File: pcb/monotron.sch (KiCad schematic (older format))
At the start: 44 parts, among them J1 Mono / Stereo, J10 DIN-5_180degree, J11 DIN-5_180degree, J12 DB9_Male, J2 Jack-DC, J3 01x07 SD Interface, J4 AudioJack3, J5 DB9_Male, J6 1x4 I2C Expansion Connector, J7 DB15_Female_HighDensity_Mount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, J8 2x6 UART Bridge, J9 DIN-5_180degree, U1 TM4C123G_Launchpad, U2 MAX3232, U3 74LS14, U4 6N138

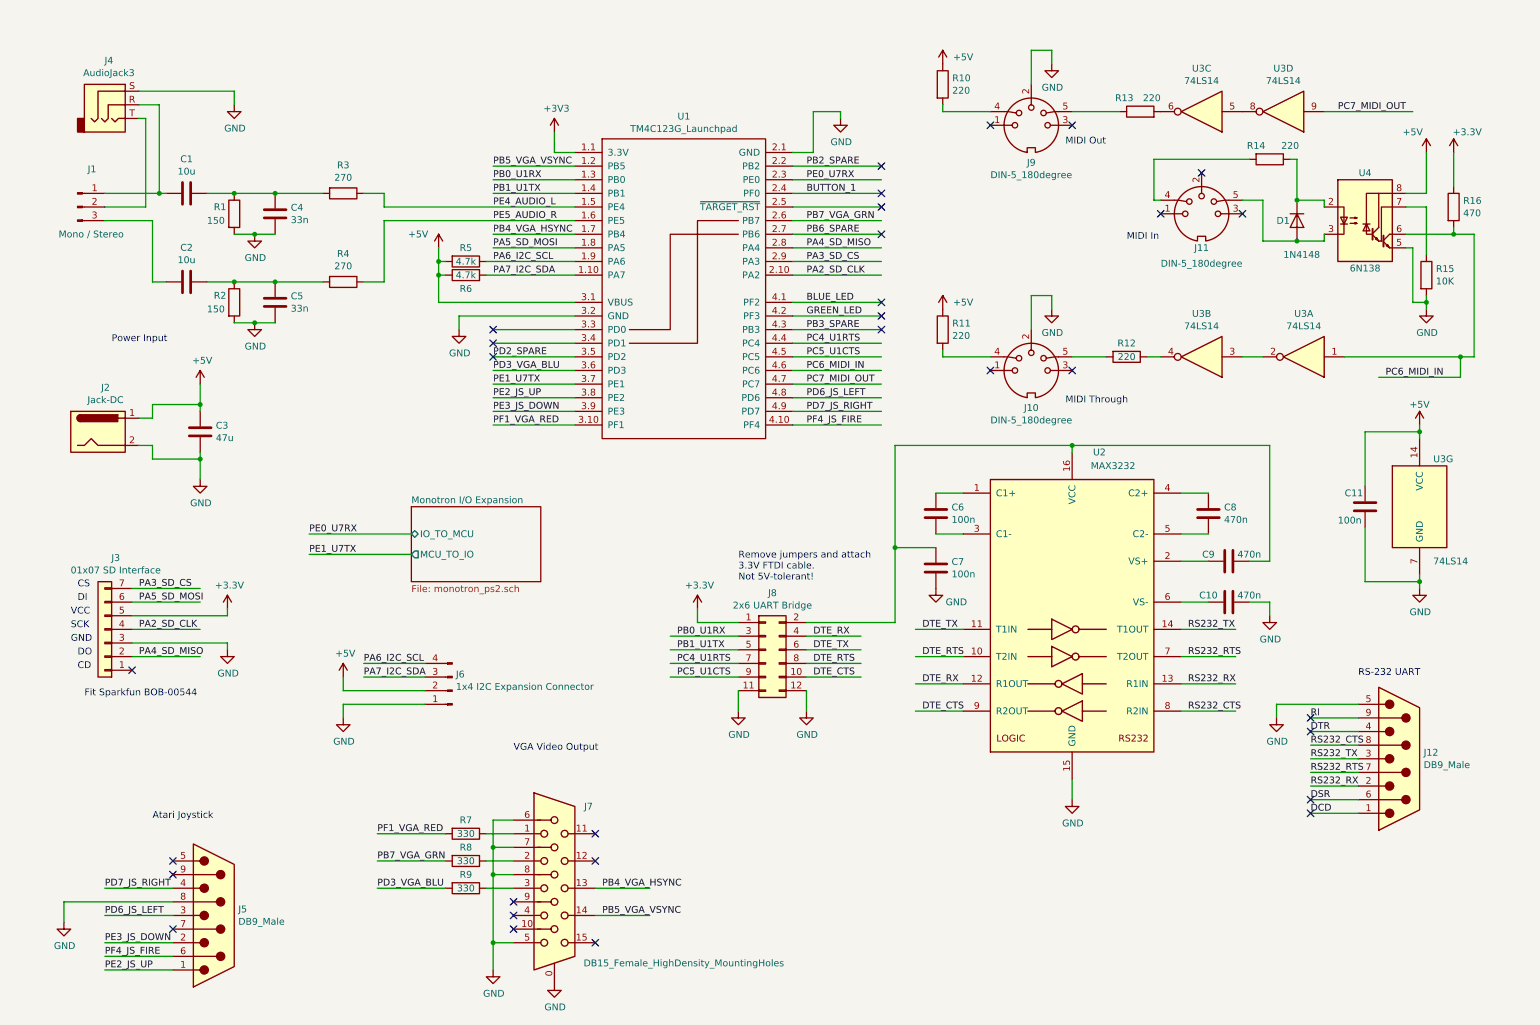
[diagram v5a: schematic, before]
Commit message: Updated footprints.
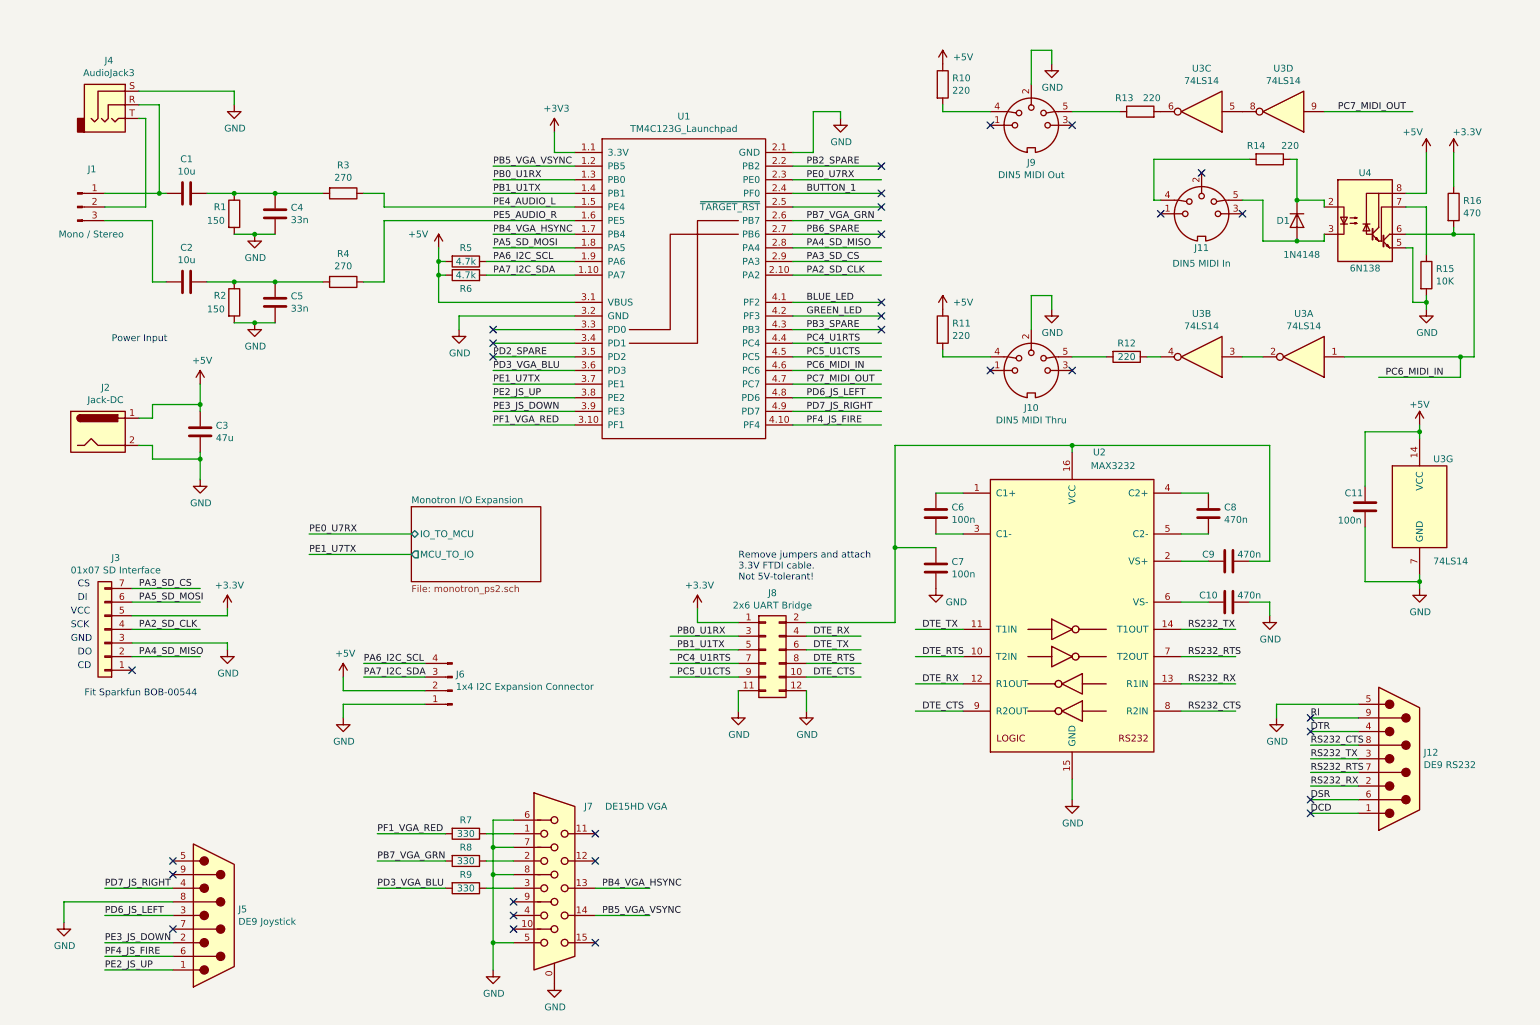
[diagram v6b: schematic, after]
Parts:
- D1: footprint (none) -> Diode_THT:D_A-405_P12.70mm_Horizontal
- J10: value DIN-5_180degree -> DIN5 MIDI Thru; footprint (none) -> Launchpad:5P180 DIN Socket
- J11: value DIN-5_180degree -> DIN5 MIDI In; footprint (none) -> Launchpad:5P180 DIN Socket
- J12: value DB9_Male -> DE9 RS232
- J4: Digikey (none) -> CP1-3533NG-ND‎
- J5: value DB9_Male -> DE9 Joystick
- J7: value DB15_Female_HighDensity_MountingHoles -> DE15HD VGA
- J9: value DIN-5_180degree -> DIN5 MIDI Out; footprint (none) -> Launchpad:5P180 DIN Socket
- R10, R11, R12, R13, R14, R15, R16: footprint (none) -> Resistor_THT:R_Axial_DIN0411_L9.9mm_D3.6mm_P12.70mm_Horizontal
- U3: footprint (none) -> Package_DIP:DIP-14_W7.62mm; Digikey (none) -> 296-1643-5-ND
- U3: footprint (none) -> Package_DIP:DIP-14_W7.62mm
- U4: footprint (none) -> Package_DIP:DIP-8_W7.62mm
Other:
- note removed: "Atari Joystick"
- note removed: "MIDI In"
- note removed: "MIDI Out"
- note removed: "MIDI Through"
- note removed: "RS-232 UART"
- note removed: "VGA Video Output"
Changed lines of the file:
@@
 P 1850 6900
 F 0 "J5" H 2030 6946 50  0000 L CNN
-F 1 "DB9_Male" H 2030 6855 50  0000 L CNN
+F 1 "DE9 Joystick" H 2030 6855 50  0000 L CNN
 F 2 "Connector_Dsub:DSUB-9_Male_Horizontal_P2.77x2.84mm_EdgePinOffset7.70mm_Housed_MountingHolesOffset9.12mm" H 1850 6900 50  0001 C CNN
 F 3 " http://portal.fciconnect.com/Comergent//fci/drawing/c-dd-0024.pdf" H 1850 6900 50  0001 C CNN
@@
 	1    0    0    -1
 $EndComp
-Text Notes 1400 6200 0    50   ~ 0
-Atari Joystick
 Text Label 1050 7300 0    50   ~ 0
 PE2_JS_UP
@@
 P 4350 6700
 F 0 "J7" H 4600 7300 50  0000 C CNN
-F 1 "DB15_Female_HighDensity_MountingHoles" H 5300 6150 50  0000 C CNN
+F 1 "DE15HD VGA" H 4950 7300 50  0000 C CNN
 F 2 "Connector_Dsub:DSUB-15-HD_Female_Horizontal_P2.29x1.98mm_EdgePinOffset8.35mm_Housed_MountingHolesOffset10.89mm" H 3400 7100 50  0001 C CNN
 F 3 "https://www.amphenol-icc.com/media/wysiwyg/files/drawing/c-cd-0012.pdf" H 3400 7100 50  0001 C CNN
@@
 F 2 "Connector_Audio:Jack_3.5mm_CUI_SJ1-3533NG_Horizontal" H 1100 950 50  0001 C CNN
 F 3 "~" H 1100 950 50  0001 C CNN
+F 4 "CP1-3533NG-ND‎" H 1100 950 50  0001 C CNN "Digikey"
 	1    1100 950
 	1    0    0    -1
@@
 AR Path="/5C4BB195" Ref="J12"  Part="1"
 F 0 "J12" H 10730 5796 50  0000 L CNN
-F 1 "DB9_Male" H 10730 5705 50  0000 L CNN
+F 1 "DE9 RS232" H 10730 5705 50  0000 L CNN
 F 2 "Connector_Dsub:DSUB-9_Male_Horizontal_P2.77x2.84mm_EdgePinOffset7.70mm_Housed_MountingHolesOffset9.12mm" H 10550 5750 50  0001 C CNN
 F 3 "http://portal.fciconnect.com/Comergent//fci/drawing/c-dd-0024.pdf" H 10550 5750 50  0001 C CNN
@@
 Text Notes 5700 4450 0    50   ~ 0
 Remove jumpers and attach\n3.3V FTDI cable.\nNot 5V-tolerant!
-Text Notes 4050 5700 0    50   ~ 0
-VGA Video Output
-Text Notes 10250 5150 0    50   ~ 0
-RS-232 UART
 Text Label 3900 2800 0    50   ~ 0
 PD2_SPARE
@@
 P 7850 1100
 F 0 "J9" H 7850 826 50  0000 C CNN
-F 1 "DIN-5_180degree" H 7850 735 50  0000 C CNN
-F 2 "" H 7850 1100 50  0001 C CNN
-F 3 "http://www.mouser.com/ds/2/18/40_c091_abd_e-75918.pdf" H 7850 1100 50  0001 C CNN
+F 1 "DIN5 MIDI Out" H 7850 735 50  0000 C CNN
+F 2 "Launchpad:5P180 DIN Socket" H 7850 1100 50  0001 C CNN
+F 3 "https://uk.rs-online.com/web/p/din-connectors/0491087/" H 7850 1100 50  0001 C CNN
 	1    7850 1100
 	1    0    0    -1
@@
 P 9100 1750
 F 0 "J11" H 9100 1500 50  0000 C CNN
-F 1 "DIN-5_180degree" H 9100 1385 50  0000 C CNN
-F 2 "" H 9100 1750 50  0001 C CNN
-F 3 "http://www.mouser.com/ds/2/18/40_c091_abd_e-75918.pdf" H 9100 1750 50  0001 C CNN
+F 1 "DIN5 MIDI In" H 9100 1385 50  0000 C CNN
+F 2 "Launchpad:5P180 DIN Socket" H 9100 1750 50  0001 C CNN
+F 3 "https://uk.rs-online.com/web/p/din-connectors/0491087/" H 9100 1750 50  0001 C CNN
 	1    9100 1750
 	1    0    0    -1
 $EndComp
-Text Notes 8100 1250 0    50   ~ 0
-MIDI Out
-Text Notes 8550 1950 0    50   ~ 0
-MIDI In
 $Comp
 L Connector:DIN-5_180degree J10
@@
 P 7850 2900
 F 0 "J10" H 7850 2626 50  0000 C CNN
-F 1 "DIN-5_180degree" H 7850 2535 50  0000 C CNN
-F 2 "" H 7850 2900 50  0001 C CNN
-F 3 "http://www.mouser.com/ds/2/18/40_c091_abd_e-75918.pdf" H 7850 2900 50  0001 C CNN
+F 1 "DIN5 MIDI Thru" H 7850 2535 50  0000 C CNN
+F 2 "Launchpad:5P180 DIN Socket" H 7850 2900 50  0001 C CNN
+F 3 "https://uk.rs-online.com/web/p/din-connectors/0491087/" H 7850 2900 50  0001 C CNN
 	1    7850 2900
 	1    0    0    -1
 $EndComp
-Text Notes 8100 3150 0    50   ~ 0
-MIDI Through
 NoConn ~ 7550 2900
 NoConn ~ 8150 2900
@@
 F 0 "R11" H 7270 2646 50  0000 L CNN
 F 1 "220" H 7270 2555 50  0000 L CNN
-F 2 "" V 7130 2600 50  0001 C CNN
+F 2 "Resistor_THT:R_Axial_DIN0411_L9.9mm_D3.6mm_P12.70mm_Horizontal" V 7130 2600 50  0001 C CNN
 F 3 "~" H 7200 2600 50  0001 C CNN
 	1    7200 2600
@@
 F 0 "R10" H 7270 846 50  0000 L CNN
 F 1 "220" H 7270 755 50  0000 L CNN
-F 2 "" V 7130 800 50  0001 C CNN
+F 2 "Resistor_THT:R_Axial_DIN0411_L9.9mm_D3.6mm_P12.70mm_Horizontal" V 7130 800 50  0001 C CNN
 F 3 "~" H 7200 800 50  0001 C CNN
 	1    7200 800
@@
 F 0 "U4" H 10300 2150 50  0000 C CNN
 F 1 "6N138" H 10300 1450 50  0000 C CNN
-F 2 "" H 10590 1500 50  0001 C CNN
+F 2 "Package_DIP:DIP-8_W7.62mm" H 10590 1500 50  0001 C CNN
 F 3 "http://www.onsemi.com/pub/Collateral/HCPL2731-D.pdf" H 10590 1500 50  0001 C CNN
 	1    10300 1800
@@
 F 0 "R14" V 9500 1250 50  0000 C CNN
 F 1 "220" V 9500 1500 50  0000 C CNN
-F 2 "" V 9530 1350 50  0001 C CNN
+F 2 "Resistor_THT:R_Axial_DIN0411_L9.9mm_D3.6mm_P12.70mm_Horizontal" V 9530 1350 50  0001 C CNN
 F 3 "~" H 9600 1350 50  0001 C CNN
 	1    9600 1350
@@
 F 0 "D1" V 9800 1650 50  0000 L CNN
 F 1 "1N4148" V 10050 1700 50  0000 L CNN
-F 2 "" H 9800 1800 50  0001 C CNN
+F 2 "Diode_THT:D_A-405_P12.70mm_Horizontal" H 9800 1800 50  0001 C CNN
 F 3 "~" H 9800 1800 50  0001 C CNN
 	1    9800 1800
@@
 F 0 "R15" H 10820 2246 50  0000 L CNN
 F 1 "10K" H 10820 2155 50  0000 L CNN
-F 2 "" V 10680 2200 50  0001 C CNN
+F 2 "Resistor_THT:R_Axial_DIN0411_L9.9mm_D3.6mm_P12.70mm_Horizontal" V 10680 2200 50  0001 C CNN
 F 3 "~" H 10750 2200 50  0001 C CNN
 	1    10750 2200
@@
 F 0 "R16" H 11020 1746 50  0000 L CNN
 F 1 "470" H 11020 1655 50  0000 L CNN
-F 2 "" V 10880 1700 50  0001 C CNN
+F 2 "Resistor_THT:R_Axial_DIN0411_L9.9mm_D3.6mm_P12.70mm_Horizontal" V 10880 1700 50  0001 C CNN
 F 3 "~" H 10950 1700 50  0001 C CNN
 	1    10950 1700
@@
 F 0 "U3" H 9850 2483 50  0000 C CNN
 F 1 "74LS14" H 9850 2574 50  0000 C CNN
-F 2 "" H 9850 2800 50  0001 C CNN
+F 2 "Package_DIP:DIP-14_W7.62mm" H 9850 2800 50  0001 C CNN
 F 3 "http://www.ti.com/lit/gpn/sn74LS14" H 9850 2800 50  0001 C CNN
+F 4 "296-1643-5-ND" H 9850 2800 50  0001 C CNN "Digikey"
 	1    9850 2800
 	-1   0    0    1
@@
 F 0 "U3" H 9100 2483 50  0000 C CNN
 F 1 "74LS14" H 9100 2574 50  0000 C CNN
-F 2 "" H 9100 2800 50  0001 C CNN
+F 2 "Package_DIP:DIP-14_W7.62mm" H 9100 2800 50  0001 C CNN
 F 3 "http://www.ti.com/lit/gpn/sn74LS14" H 9100 2800 50  0001 C CNN
 	2    9100 2800
@@
 F 0 "R12" V 8450 2800 50  0000 C CNN
 F 1 "220" V 8550 2800 50  0000 C CNN
-F 2 "" V 8480 2800 50  0001 C CNN
+F 2 "Resistor_THT:R_Axial_DIN0411_L9.9mm_D3.6mm_P12.70mm_Horizontal" V 8480 2800 50  0001 C CNN
 F 3 "~" H 8550 2800 50  0001 C CNN
 	1    8550 2800
@@
 F 0 "U3" H 10800 4250 50  0000 L CNN
 F 1 "74LS14" H 10800 3500 50  0000 L CNN
-F 2 "" H 10700 3900 50  0001 C CNN
+F 2 "Package_DIP:DIP-14_W7.62mm" H 10700 3900 50  0001 C CNN
 F 3 "http://www.ti.com/lit/gpn/sn74LS14" H 10700 3900 50  0001 C CNN
 	7    10700 3900
@@
 F 0 "R13" V 8750 1050 50  0000 L CNN
 F 1 "220" V 8750 850 50  0000 L CNN
-F 2 "" V 8580 1000 50  0001 C CNN
+F 2 "Resistor_THT:R_Axial_DIN0411_L9.9mm_D3.6mm_P12.70mm_Horizontal" V 8580 1000 50  0001 C CNN
 F 3 "~" H 8650 1000 50  0001 C CNN
 	1    8650 1000
@@
 F 0 "U3" H 9100 683 50  0000 C CNN
 F 1 "74LS14" H 9100 774 50  0000 C CNN
-F 2 "" H 9100 1000 50  0001 C CNN
+F 2 "Package_DIP:DIP-14_W7.62mm" H 9100 1000 50  0001 C CNN
 F 3 "http://www.ti.com/lit/gpn/sn74LS14" H 9100 1000 50  0001 C CNN
 	3    9100 1000
@@
 F 0 "U3" H 9700 683 50  0000 C CNN
 F 1 "74LS14" H 9700 774 50  0000 C CNN
-F 2 "" H 9700 1000 50  0001 C CNN
+F 2 "Package_DIP:DIP-14_W7.62mm" H 9700 1000 50  0001 C CNN
 F 3 "http://www.ti.com/lit/gpn/sn74LS14" H 9700 1000 50  0001 C CNN
 	4    9700 1000

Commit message: Shrunk board a little (components can hang off edge). Relabelled parts to generic names.
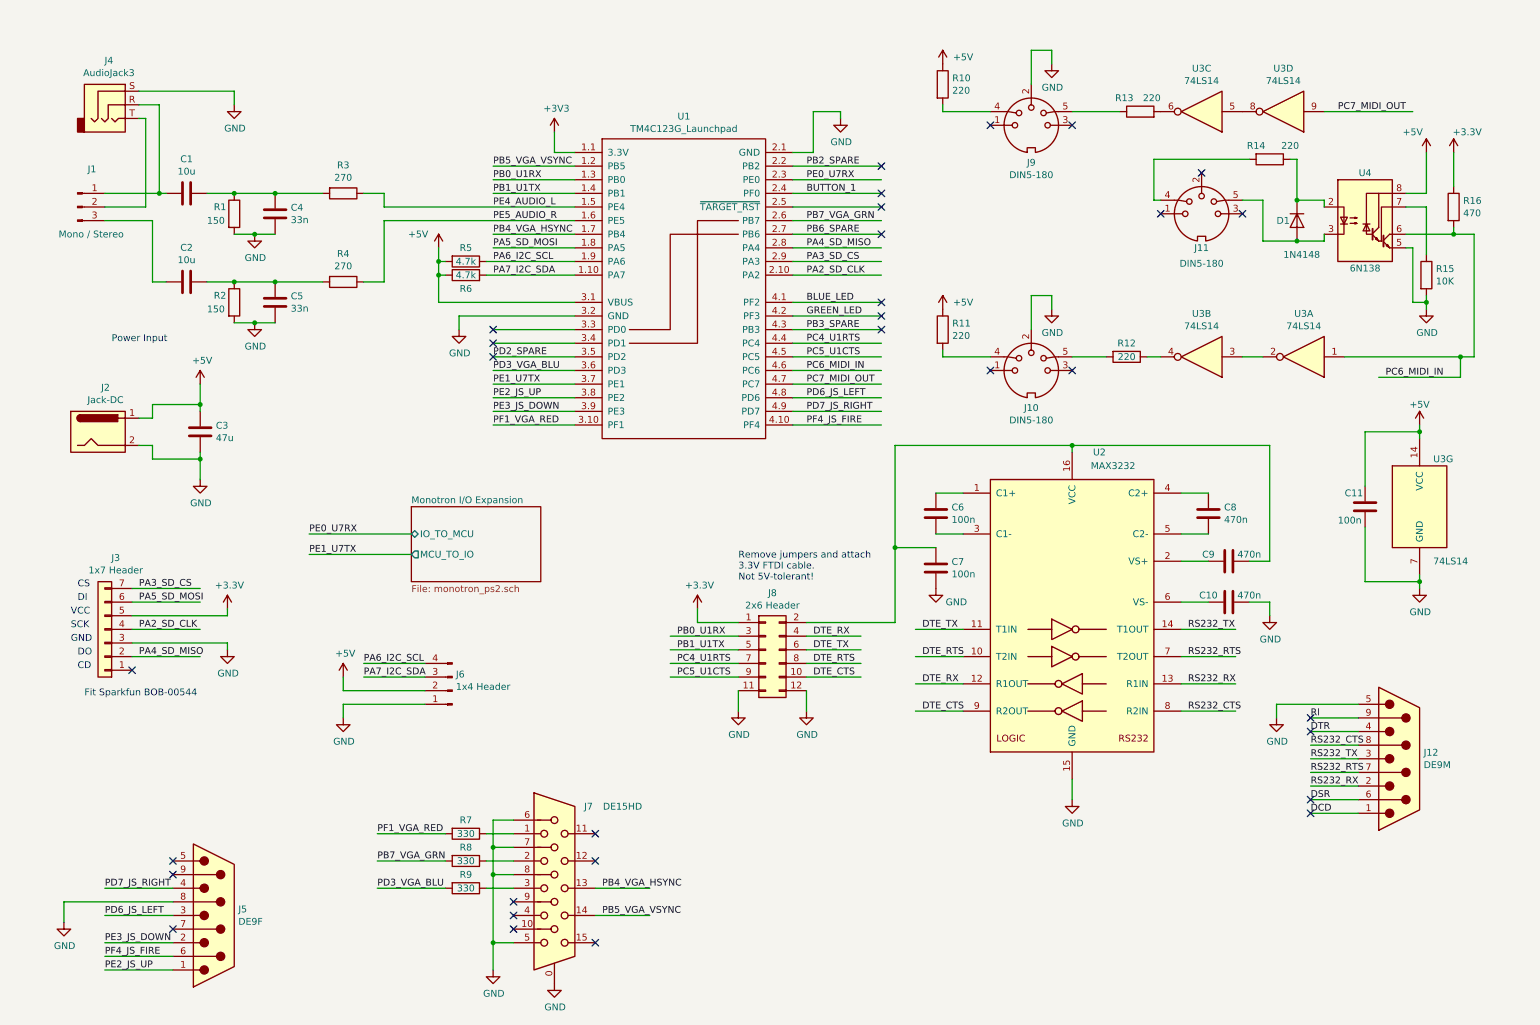
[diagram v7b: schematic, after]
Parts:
- J10: value DIN5 MIDI Thru -> DIN5-180
- J11: value DIN5 MIDI In -> DIN5-180
- J12: value DE9 RS232 -> DE9M
- J3: value 01x07 SD Interface -> 1x7 Header
- J5: value DE9 Joystick -> DE9F
- J6: value 1x4 I2C Expansion Connector -> 1x4 Header
- J7: value DE15HD VGA -> DE15HD
- J8: value 2x6 UART Bridge -> 2x6 Header
- J9: value DIN5 MIDI Out -> DIN5-180
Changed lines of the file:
@@
 P 1850 6900
 F 0 "J5" H 2030 6946 50  0000 L CNN
-F 1 "DE9 Joystick" H 2030 6855 50  0000 L CNN
+F 1 "DE9F" H 2030 6855 50  0000 L CNN
 F 2 "Connector_Dsub:DSUB-9_Male_Horizontal_P2.77x2.84mm_EdgePinOffset7.70mm_Housed_MountingHolesOffset9.12mm" H 1850 6900 50  0001 C CNN
 F 3 " http://portal.fciconnect.com/Comergent//fci/drawing/c-dd-0024.pdf" H 1850 6900 50  0001 C CNN
@@
 P 4350 6700
 F 0 "J7" H 4600 7300 50  0000 C CNN
-F 1 "DE15HD VGA" H 4950 7300 50  0000 C CNN
+F 1 "DE15HD" H 4850 7300 50  0000 C CNN
 F 2 "Connector_Dsub:DSUB-15-HD_Female_Horizontal_P2.29x1.98mm_EdgePinOffset8.35mm_Housed_MountingHolesOffset10.89mm" H 3400 7100 50  0001 C CNN
 F 3 "https://www.amphenol-icc.com/media/wysiwyg/files/drawing/c-cd-0012.pdf" H 3400 7100 50  0001 C CNN
@@
 P 5900 4950
 F 0 "J8" H 5950 5367 50  0000 C CNN
-F 1 "2x6 UART Bridge" H 5950 5276 50  0000 C CNN
+F 1 "2x6 Header" H 5950 5276 50  0000 C CNN
 F 2 "Connector_PinHeader_2.54mm:PinHeader_2x06_P2.54mm_Vertical" H 5900 4950 50  0001 C CNN
 F 3 "~" H 5900 4950 50  0001 C CNN
@@
 P 3600 5250
 F 0 "J6" H 3573 5130 50  0000 R CNN
-F 1 "1x4 I2C Expansion Connector" H 3573 5221 50  0000 R CNN
+F 1 "1x4 Header" H 3573 5221 50  0000 R CNN
 F 2 "Connector_PinHeader_2.54mm:PinHeader_1x04_P2.54mm_Vertical" H 3600 5250 50  0001 C CNN
 F 3 "~" H 3600 5250 50  0001 C CNN
@@
 P 1050 4800
 F 0 "J3" H 970 4275 50  0000 C CNN
-F 1 "01x07 SD Interface" H 970 4366 50  0000 C CNN
+F 1 "1x7 Header" H 970 4366 50  0000 C CNN
 F 2 "Connector_PinHeader_2.54mm:PinHeader_1x07_P2.54mm_Vertical" H 1050 4800 50  0001 C CNN
 F 3 "~" H 1050 4800 50  0001 C CNN
@@
 AR Path="/5C4BB195" Ref="J12"  Part="1"
 F 0 "J12" H 10730 5796 50  0000 L CNN
-F 1 "DE9 RS232" H 10730 5705 50  0000 L CNN
+F 1 "DE9M" H 10730 5705 50  0000 L CNN
 F 2 "Connector_Dsub:DSUB-9_Male_Horizontal_P2.77x2.84mm_EdgePinOffset7.70mm_Housed_MountingHolesOffset9.12mm" H 10550 5750 50  0001 C CNN
 F 3 "http://portal.fciconnect.com/Comergent//fci/drawing/c-dd-0024.pdf" H 10550 5750 50  0001 C CNN
@@
 P 7850 1100
 F 0 "J9" H 7850 826 50  0000 C CNN
-F 1 "DIN5 MIDI Out" H 7850 735 50  0000 C CNN
+F 1 "DIN5-180" H 7850 735 50  0000 C CNN
 F 2 "Launchpad:5P180 DIN Socket" H 7850 1100 50  0001 C CNN
 F 3 "https://uk.rs-online.com/web/p/din-connectors/0491087/" H 7850 1100 50  0001 C CNN
@@
 P 9100 1750
 F 0 "J11" H 9100 1500 50  0000 C CNN
-F 1 "DIN5 MIDI In" H 9100 1385 50  0000 C CNN
+F 1 "DIN5-180" H 9100 1385 50  0000 C CNN
 F 2 "Launchpad:5P180 DIN Socket" H 9100 1750 50  0001 C CNN
 F 3 "https://uk.rs-online.com/web/p/din-connectors/0491087/" H 9100 1750 50  0001 C CNN
@@
 P 7850 2900
 F 0 "J10" H 7850 2626 50  0000 C CNN
-F 1 "DIN5 MIDI Thru" H 7850 2535 50  0000 C CNN
+F 1 "DIN5-180" H 7850 2535 50  0000 C CNN
 F 2 "Launchpad:5P180 DIN Socket" H 7850 2900 50  0001 C CNN
 F 3 "https://uk.rs-online.com/web/p/din-connectors/0491087/" H 7850 2900 50  0001 C CNN
